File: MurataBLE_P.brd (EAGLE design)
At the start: 90 x 70 mm, 89 parts, among them CON1 C-2235, CON2 C-2235, IC1 I-5448, IC3 74LVC1G00DBV, IC5 I-5448, IC6 74LVC1G00DBV, Q1 FC-135 32.7680KA-AG3, Q2 12MHz, Q3 FC-135 32.7680KA-AG3, Q4 12MHz, SW1 P8073, SW2 P8073, SW3 P8073, SW4 P8073, SW5 P8073, SW6 P8073, U1 IC_BLE_LBCA2HNZYZ-711, U2 IC_BLE_LBCA2HNZYZ-711, X1 TSW-114-02-S-S, X2 TSW-114-02-S-S

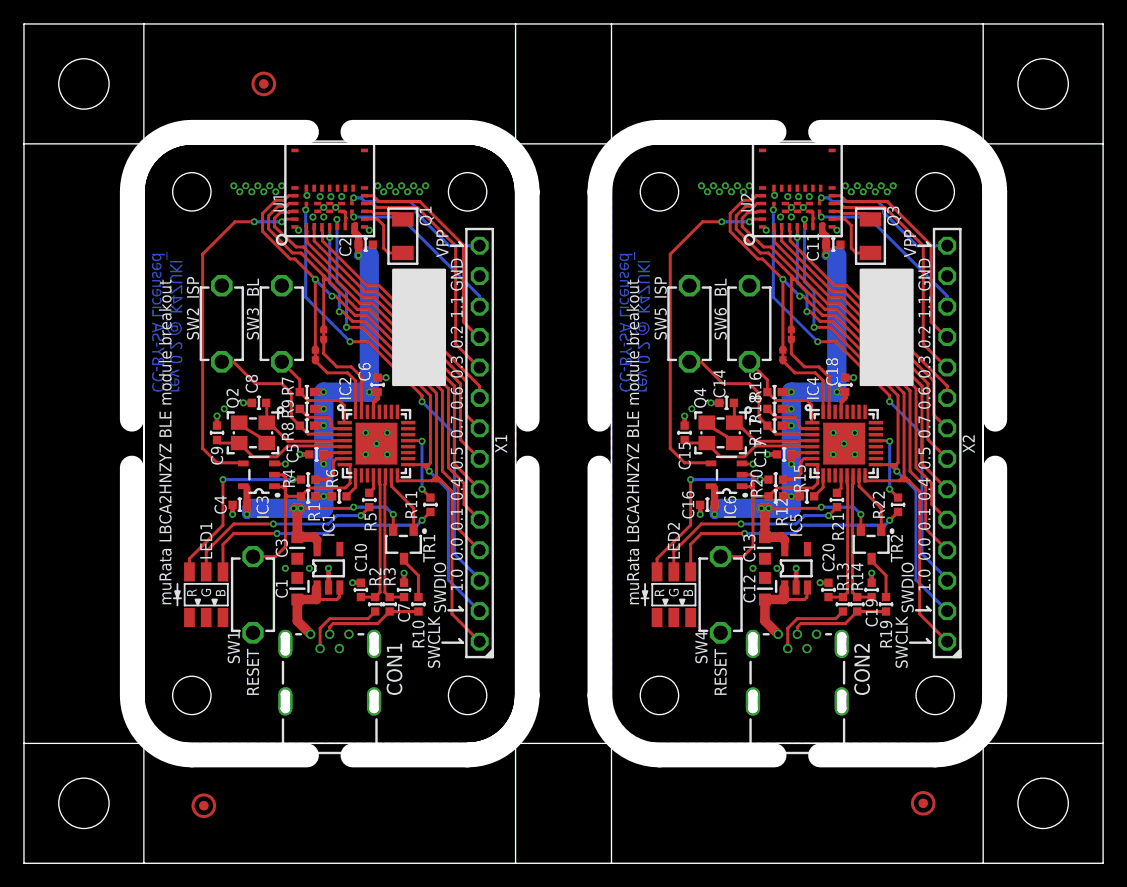
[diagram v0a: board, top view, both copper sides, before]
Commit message: [ USB ]add values; panelized
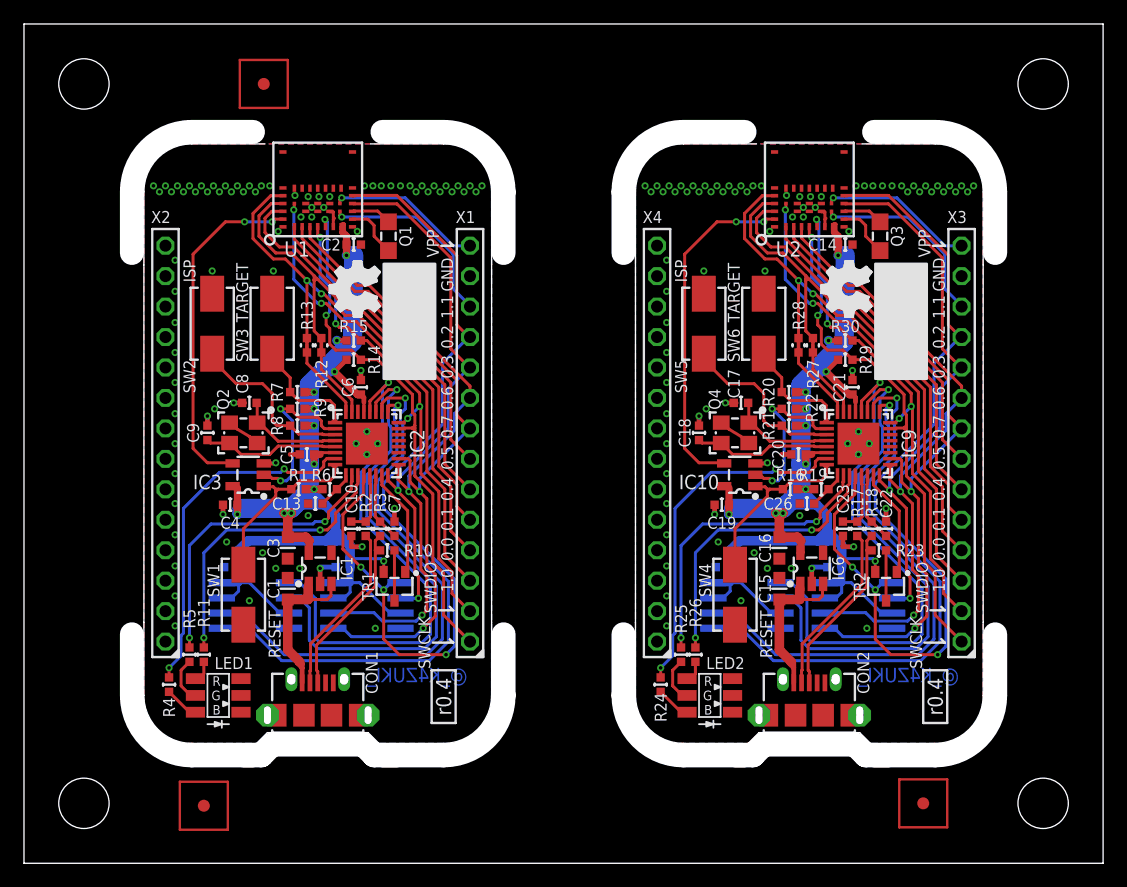
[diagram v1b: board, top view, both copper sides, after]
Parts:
- removed PCB1, PCB2: PCB_DP_RECTANGLE-31X50, dp_pcb:DP5031_V1
- removed TP1, TP16, TP17, TP18, TP19, TP2, TP3, TP4: TESTPAD, mylib:TP06RECT
- removed TP10, TP11, TP9: TPTP08R, testpad_local:TP08R
- removed TP12, TP13, TP14, TP15, TP5, TP6, TP7, TP8: TPTP06R, testpad_local:TP06R
- added C21, C24, C25, C26: 0.1u/1005, mylib:C0402
- added C22, C23: 18p/1005, mylib:C0402
- added GIT1: (no value), git-revision:GIT-REVISION
- added IC10: (no value), mylib:SOT95P280X145-5N
- added IC7, IC8: (no value), mylib:IC_08_1.27_150MIL
- added IC9: (no value), mylib:HVQFN33
- added ICON1, ICON3: r0.4, mylib:ICON_REVISION1.2
- added ICON2, ICON4: (no value), mylib:ICON_OSHW
- added P1, P2, P3, P4, P5, P6, P7, P8: (no value), mylib:PCB_CORNER_NH
- added R23: 1.5k/1005, mylib:C0402
- added R24, R25, R26: (no value), mylib:C0402
- added R27, R28: (no value), mylib:R0402SHORT
- added R29, R30: 10k/1005, mylib:C0402
- added TP100, TP101, TP102: TESTPAD_F, mylib:FIDUCIAL
- added X3, X4: TSW-114-02-S-S, mylib:TSW-114-07-F-S
- C12, C13: value 1u/1608 -> 0.1u/1005; device mylib:CR_1608 -> mylib:C0402
- C14, C19, C20: value 18p/1005 -> 0.1u/1005
- C15: value 18p/1005 -> 1u/1608; device mylib:C0402 -> mylib:CR_1608
- C16: value 0.1u/1005 -> 1u/1608; device mylib:C0402 -> mylib:CR_1608
- C17, C18: value 0.1u/1005 -> 18p/1005
- CON1, CON2: value C-2235 -> (none); device mylib:CON_USB_MINIB_AKI -> mylib:CON_USB_47589-0001MOLEX
- IC1: device mylib:IC_05_0.95_50MIL -> mylib:SOT95P280X145-5N
- IC3: value 74LVC1G00DBV -> (none); device 74xx-little-us_local:SOT23-5 -> mylib:SOT95P280X145-5N
- IC4: device mylib:HVQFN33 -> mylib:IC_08_1.27_150MIL
- IC5: value I-5448 -> (none); device mylib:IC_05_0.95_50MIL -> mylib:IC_08_1.27_150MIL
- IC6: value 74LVC1G00DBV -> I-5448; device 74xx-little-us_local:SOT23-5 -> mylib:SOT95P280X145-5N
- Q1, Q3: value FC-135 32.7680KA-AG3 -> (none); device mylib:CRYSTAL_FC-135 -> mylib:CR_2125
- Q2, Q4: value 12MHz -> (none); device adafruit (1):NX3225 -> mylib:CLOCK_3225
- R11, R5: value 75/1005 -> (none)
- R12: value 10k/1005 -> (none); device mylib:C0402 -> mylib:R0402SHORT
- R13: value 33/1005 -> (none); device mylib:C0402 -> mylib:R0402SHORT
- R14: value 33/1005 -> 10k/1005
- R17, R18: value 10k/1005 -> 33/1005
- R19: value 1.5k/1005 -> 10k/1005
- R20: value 270/1005 -> 10k/1005
- R21, R22: value 75/1005 -> 10k/1005
- R4: value 270/1005 -> (none)
- SW1, SW2, SW3, SW4, SW5, SW6: value P8073 -> (none); device mylib:SW_TACTSW_P8073 -> mylib:SW_TACTSW_FSM2JMTR
- TR1, TR2: value I-4269 -> PMOS_BSS84_SOT23
- U1, U2: value IC_BLE_LBCA2HNZYZ-711 -> (none)
- X1, X2: device mylib:TSW-114-02-S-S -> mylib:TSW-114-07-F-S
- moved X2 65.2 mm to (11.8, 35.0)
- moved IC4 50.9 mm to (19.3, 21.5), flipped to the bottom, turned to 270 degrees
- moved R13 49.6 mm to (23.6, 43.2)
- moved C11 49.0 mm to (26.6, 24.7), flipped to the bottom
- moved R14 46.7 mm to (27.5, 42.0), turned to 180 degrees
- moved C12 44.5 mm to (17.3, 24.7), flipped to the bottom, turned to 0 degrees
- moved R15 40.0 mm to (27.5, 43.6), turned to 180 degrees
- moved R12 39.9 mm to (24.8, 43.2), turned to 90 degrees
- moved C13 37.7 mm to (24.3, 30.0), turned to 180 degrees
- moved IC5 35.9 mm to (28.6, 21.5), flipped to the bottom, turned to 270 degrees
- moved R11 22.7 mm to (15.0, 17.4)
- moved R4 20.7 mm to (12.1, 14.9), turned to 270 degrees
- moved R5 19.8 mm to (13.8, 17.4)
- moved C14 16.5 mm to (68.5, 51.6), turned to 0 degrees
- moved C15 15.2 mm to (63.0, 22.9)
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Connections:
- net P0_4 renamed 580.P0_4
- net P0_5 renamed 580.P0_5
- net P1_0 renamed 580.P1_0
- removed net P0_10: U2.12, X2.11
- removed net P0_11: U2.11, X2.10
- removed net P0_12: U2.24, X2.6
- removed net P0_6: U1.3, X1.9
- removed net P0_7: U1.2, X1.8
- removed net P0_8: U2.3, X2.9
- removed net P0_9: U2.2, X2.8
- removed net P1_2: U2.35, X2.3
- removed net P1_3: U2.30, X2.12
- new net 580.P0_0: R12.3, U1.23, X1.5
- new net 580.P0_1: R13.3, U1.22, X1.4
- new net 580.P0_10: IC8.5, IC9.18, U2.2, X3.8
- new net 580.P0_11: IC8.1, IC9.12, U2.12, X3.11
- new net 580.P0_12: IC8.2, IC9.16, U2.11, X3.10
- new net 580.P0_13: U2.24, X3.6
- new net 580.P0_14: R27.3, U2.23, X3.5
- new net 580.P0_15: R28.3, U2.22, X3.4
- new net 580.P0_2: IC2.12, IC5.1, U1.12, X1.11
- new net 580.P0_3: IC2.16, IC5.2, U1.11, X1.10
- new net 580.P0_6: IC2.17, IC5.6, U1.3, X1.9
- new net 580.P0_7: IC2.18, IC5.5, U1.2, X1.8
- new net 580.P0_8: U2.1, X3.7
- new net 580.P0_9: IC8.6, IC9.17, U2.3, X3.9
- new net 580.P1_1: U1.30, X1.12
- new net 580.P1_2: U2.35, X3.3
- new net 580.P1_3: U2.30, X3.12
- new net P0_15: IC2.25, IC4.6
- new net P0_16: IC2.26, IC4.5
- new net P0_32: IC2.27, IC4.2
- new net P1_15: IC2.28, IC4.1
- net !RESET!: now also SW1.2; no longer IC3.2, SW1.A2
- net !RESET!1: now also IC10.1, IC9.8, R16.2, SW4.2; no longer IC4.8, IC6.1, IC6.2, R12.2, SW4.A2
- net 3.3V: now also C11.1, C12.1, IC4.3, IC4.7, IC4.8, IC5.3, IC5.7, IC5.8, R14.2, R15.2
- net 3.3V1: now also C14.1, C19.1, C20.1, C21.1, C24.1, C25.1, IC10.5, IC7.3, IC7.7, IC7.8, IC8.3, IC8.7, IC8.8, IC9.29, IC9.6, R19.1, R20.1, R21.1, R22.1, R29.2, R30.2; no longer C11.1, C13.1, C17.1, C18.1, IC4.29, IC4.6, IC5.5, R12.1, R15.1, R17.1, R18.1
- net FB_BL: now also SW3.2; no longer SW3.A2
- net FB_BL1: now also IC9.1, R20.2, SW6.2; no longer IC4.1, R16.2, SW6.A2
- net FB_ISP: now also SW2.2; no longer SW2.A2
- net FB_ISP1: now also IC9.3, R21.2, SW5.2; no longer IC4.3, R17.2, SW5.A2
- net GND: now also C11.2, C12.2, C13.2, CON1.5, CON1.SHD, CON1.SHD$1, CON1.SHD$2, CON1.SHD$3, CON1.SHD$4, CON1.SHD$5, CON1.SHD$6, CON1.SHD$7, IC4.4, IC5.4, SW1.1, SW2.1, SW3.1; no longer CON1.GND, SW1.A1, SW2.A1, SW3.A1
- net GND1: now also C21.2, C22.2, C23.2, C24.2, C25.2, C26.2, CON2.5, CON2.SHD, CON2.SHD$1, CON2.SHD$2, CON2.SHD$3, CON2.SHD$4, CON2.SHD$5, CON2.SHD$6, CON2.SHD$7, IC10.3, IC6.2, IC7.4, IC8.4, IC9.EXP, SW4.1, SW5.1, SW6.1, X3.13; no longer C11.2, C12.2, C13.2, CON2.GND, IC4.EXP, IC5.2, IC6.3, SW4.A1, SW5.A1, SW6.A1, X2.13
- net N$10: now also IC2.11; no longer IC2.21
- net N$16: now also C17.1, IC9.4; no longer C14.1, IC4.4
- net N$17: now also C18.1, IC9.5; no longer C15.1, IC4.5
- net N$21: now also CON1.3; no longer CON1.D+
- net N$22: now also CON1.2; no longer CON1.D-
- net N$23: now also CON2.3, R18.1, R23.2; no longer CON2.D+, R14.1, R19.2
- net N$25: now also CON2.2, R17.1; no longer CON2.D-, R13.1
- net N$26: now also C22.1, IC9.14, R18.2; no longer C19.1, IC4.14, R14.2
- net N$27: now also C23.1, IC9.13, R17.2; no longer C20.1, IC4.13, R13.2
- net N$28: now also C26.1, IC9.9, R19.2; no longer IC4.9, R15.2
- net N$29: now also IC10.2, IC9.2, R22.2; no longer IC4.2, R18.2
- net N$30: now also R23.1; no longer R19.1
- net N$31: now also IC9.15; no longer IC4.15
- net N$32: now also IC9.7, R24.1; no longer IC4.7, R20.1
- net N$33: now also IC9.10, R25.1; no longer IC4.12, R21.1
- net N$34: now also IC9.11, R26.1; no longer IC4.21, R22.1
- net N$35: now also R24.2; no longer R20.2
- net N$36: now also R25.2; no longer R21.2
- net N$37: now also R26.2; no longer R22.2
- net N$4: now also C13.1
- net N$5: now also IC3.2
- net N$9: now also IC2.10; no longer IC2.12
- net P0_1: now also IC7.2, IC9.27; no longer U2.1, X2.7
- net P0_2: now also IC7.5, IC9.26; no longer U1.12, X1.11
- net P0_3: now also IC7.6, IC9.25; no longer U1.11, X1.10
- net P1_1: now also IC7.1, IC9.28; no longer U1.30, X1.12
- net RESET1: now also IC10.4; no longer IC6.4
- net SWCLK: now also IC2.23, R14.1; no longer IC2.16
- net SWCLK1: now also IC9.23, R29.1, X3.1; no longer IC4.16, X2.1
- net SWDIO: now also IC2.24, R15.1; no longer IC2.17
- net SWDIO1: now also IC9.24, R30.1, X3.2; no longer IC4.17, X2.2
- net TGT_RX: now also R13.1, R13.2; no longer TP2.TP, TP4.TP, TP6.TP, TP7.TP, U1.22, X1.4
- net TGT_RX1: now also IC9.32, R28.1, R28.2; no longer IC4.32, TP13.TP, TP14.TP, TP17.TP, TP19.TP, U2.22, X2.4
- net TGT_TX: now also R12.1, R12.2; no longer TP1.TP, TP3.TP, TP5.TP, TP8.TP, U1.23, X1.5
- net TGT_TX1: now also IC9.31, R27.1, R27.2; no longer IC4.31, TP12.TP, TP15.TP, TP16.TP, TP18.TP, U2.23, X2.5
- net VPP1: now also X3.14; no longer X2.14
- net VUSB: now also CON1.1; no longer CON1.VBUS
- net VUSB1: now also C15.1, CON2.1, IC6.1, IC6.3; no longer C12.1, CON2.VBUS, IC5.1, IC5.3
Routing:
- net 580.P0_2: track 0.00 -> 73.6 mm, vias 0 -> 3
- net 580.P0_11: track 0.00 -> 73.6 mm, vias 0 -> 3
- net 580.P0_10: track 0.00 -> 54.7 mm, vias 0 -> 2
- net 580.P0_7: track 0.00 -> 54.7 mm, vias 0 -> 2
- net 580.P0_9: track 0.00 -> 52.6 mm, vias 0 -> 2
- net 580.P0_6: track 0.00 -> 52.6 mm, vias 0 -> 2
- net P0_16: track 0.00 -> 47.4 mm, vias 0 -> 1
- net TGT_RX1: track 53.3 -> 6.90 mm, vias 2 -> 0
- net TGT_RX: track 53.3 -> 6.90 mm, vias 2 -> 0
- net 580.P0_3: track 0.00 -> 45.6 mm, vias 0 -> 2
- net 580.P0_12: track 0.00 -> 45.6 mm, vias 0 -> 2
- net 580.P0_15: track 0.00 -> 44.9 mm, vias 0 -> 2
- net 580.P0_1: track 0.00 -> 44.9 mm, vias 0 -> 2
- net P0_15: track 0.00 -> 44.7 mm, vias 0 -> 1
- net P1_15: track 0.00 -> 43.7 mm, vias 0 -> 1
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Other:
- outline, holes or cut-outs redrawn
- board text added: "@_K4ZUKI_"
- board text added: "C11"
- board text added: "C12"
- board text added: "C13"
- board text added: "IC4"
- board text added: "IC5"
- board text added: "R12"
- board text added: "R13"
- board text added: "R14"
- board text added: "R15"
- board text added: "TARGET"
- board text added: "V-CUT"
- board text added: "X2"
- board text removed: "BL"
- board text removed: "CC-BY-SA Licensed"
- board text removed: "rev 0.2 @_K4ZUKI_"

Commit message: [ USB ] GERBER as per aef7891
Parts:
- added GIT2: aef7891, git-revision:GIT-REVISION
- added LED3, LED4: LED_3SEG, mylib:LED_3SEG_SMD
- added R31: NC, mylib:R0402SHORT
- added R32, R33: 10k/1005, mylib:C0402
- added R34, R35, R36: 1k/1005, mylib:C0402
- CON1, CON2: value (none) -> 47589-0001
- GIT1: value (none) -> aef7891
- IC1: value I-5448 -> (none); device mylib:SOT95P280X145-5N -> mylib:DFN80P410X410_8N
- IC10: device mylib:SOT95P280X145-5N -> mylib:DFN80P410X410_8N
- IC2: value (none) -> LPC11U35_QFN33
- IC3: value (none) -> NC7SZ00
- IC4: value (none) -> AT25DN512C
- IC5, IC7: value (none) -> AT25XE011
- IC6: value I-5448 -> AT25DN512C; device mylib:SOT95P280X145-5N -> mylib:IC_08_1.27_150MIL
- IC8: value (none) -> LPC11U35_QFN33; device mylib:IC_08_1.27_150MIL -> mylib:HVQFN33
- IC9: value (none) -> NC7SZ00; device mylib:HVQFN33 -> mylib:SOT95P280X145-5N
- ICON2, ICON4, P1, P2, P3, P4, P5, P6, P7, P8, R12, R13: value (none) -> NC
- Q1, Q3: value (none) -> 32.768K/2012
- Q2, Q4: value (none) -> 12M/3225
- R11, R4, R5: value (none) -> 1k/1005
- R16, R29: value 10k/1005 -> 1k/1005
- R17, R18: value 33/1005 -> 1k/1005
- R20, R21: value 10k/1005 -> 33/1005
- R23: value 1.5k/1005 -> 10k/1005
- R24, R25: value (none) -> 10k/1005
- R26: value (none) -> 1.5k/1005
- R27, R28: value (none) -> 1k/1005; device mylib:R0402SHORT -> mylib:C0402
- R30: value 10k/1005 -> NC; device mylib:C0402 -> mylib:R0402SHORT
- SW1, SW2, SW3, SW4, SW5, SW6: value (none) -> FSM2JMTR
- TP100, TP101, TP102: value TESTPAD_F -> NC
- TR1, TR2: value PMOS_BSS84_SOT23 -> BSS84
- U1, U2: value (none) -> LBCA2HNZYZ
- moved R18 64.3 mm to (11.9, 53.9), turned to 180 degrees
- moved R17 61.1 mm to (14.8, 55.1), turned to 180 degrees
- moved R16 57.2 mm to (11.9, 55.1)
- moved LED2 56.2 mm to (16.1, 52.4), turned to 0 degrees
- moved GIT1 35.1 mm to (32.2, 13.9), turned to 90 degrees
- moved R24 24.1 mm to (63.8, 36.5), turned to 180 degrees
- moved R27 23.5 mm to (54.8, 22.4), turned to 270 degrees
- moved R25 22.4 mm to (63.8, 37.9), turned to 180 degrees
- moved R29 20.9 mm to (56.0, 25.3), turned to 270 degrees
- moved R28 20.4 mm to (54.8, 25.3), turned to 270 degrees
- moved R26 17.6 mm to (71.3, 26.1), turned to 180 degrees
- moved R23 15.2 mm to (63.8, 39.3)
- moved IC8 13.5 mm to (69.6, 35.0), flipped to the top, turned to 0 degrees
- moved R20 12.7 mm to (69.5, 27.9), turned to 90 degrees
- moved R21 11.0 mm to (70.7, 27.9), turned to 90 degrees
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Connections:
- net VPP1 renamed VPP2
- removed net N$17 (its old number): C18.1, IC9.5, Q4.3
- removed net N$5 (its old number): IC2.2, IC3.2, R9.2
- new net N$14: LED2.3, R18.1
- new net N$15: LED2.2, R17.1
- new net N$38: LED3.3, R27.2
- new net N$39: LED4.3, R36.1
- new net N$40: LED4.2, R35.1
- new net N$41: LED4.1, R34.1
- new net NSRST: IC2.8, IC3.1, IC3.2, R1.2
- new net NSRST1: IC8.8, IC9.1, IC9.2, R19.2
- net !RESET!: now also IC2.2, R9.2; no longer IC2.8, IC3.1, R1.2
- net !RESET!1: now also IC8.2, R25.2; no longer IC10.1, IC9.8, R16.2
- net 3.3V: now also IC1.6, IC1.7, IC1.EP, LED1.4, LED1.5, LED1.6, X2.1
- net 3.3V1: now also IC10.6, IC10.7, IC10.EP, IC6.3, IC6.7, IC6.8, IC8.29, IC8.6, IC9.5, LED3.4, LED3.5, LED3.6, R23.1, R24.1, R25.1, R32.2, R33.2, X4.1; no longer IC6.5, IC8.3, IC8.7, IC8.8, IC9.29, IC9.6, R16.1, R20.1, R21.1, R29.2, R30.2
- net 580.P0_0: now also LED2.4
- net 580.P0_1: now also LED2.5
- net 580.P0_10: now also IC7.5, IC8.18; no longer IC8.5, IC9.18
- net 580.P0_11: now also IC7.1, IC8.12; no longer IC8.1, IC9.12
- net 580.P0_12: now also IC7.2, IC8.16; no longer IC8.2, IC9.16
- net 580.P0_14: now also LED4.4, R30.3; no longer R27.3
- net 580.P0_15: now also LED4.5, R31.3; no longer R28.3
- net 580.P0_9: now also IC7.6, IC8.17; no longer IC8.6, IC9.17
- net 580.P1_0: now also LED2.6
- net 580.P1_2: now also LED4.6
- net FB_BL1: now also IC8.1, R23.2; no longer IC9.1, R20.2
- net FB_ISP1: now also IC8.3, R24.2; no longer IC9.3, R21.2
- net GND: now also IC1.1, R16.2, R17.2, R18.2; no longer IC1.2, LED1.1, LED1.2, LED1.3
- net GND1: now also IC10.1, IC6.4, IC8.EXP, IC9.3, R34.2, R35.2, R36.2; no longer IC10.3, IC6.2, IC8.4, IC9.EXP, LED2.1, LED2.2, LED2.3
- net N$11: now also LED1.1, R11.2; no longer LED1.4, R4.2
- net N$12: now also LED1.2; no longer LED1.5
- net N$13: now also LED1.3, R4.2; no longer LED1.6, R11.2
- net N$16: now also LED2.1, R16.1; no longer C17.1, IC9.4, Q4.1
- net N$23: now also C17.1, IC8.4, Q4.1; no longer CON2.3, R18.1, R23.2
- net N$25: now also C18.1, IC8.5, Q4.3; no longer CON2.2, R17.1
- net N$26: now also CON2.3, R21.1, R26.2; no longer C22.1, IC9.14, R18.2
- net N$27: now also CON2.2, R20.1; no longer C23.1, IC9.13, R17.2
- net N$28: now also C22.1, IC8.14, R21.2; no longer C26.1, IC9.9, R19.2
- net N$29: now also C23.1, IC8.13, R20.2; no longer IC10.2, IC9.2, R22.2
- net N$30: now also C26.1, IC8.9, R22.2; no longer R23.1, TR2.3
- net N$31: now also R26.1, TR2.3; no longer IC9.15, TR2.1
- net N$32: now also IC8.15, TR2.1; no longer IC9.7, R24.1
- net N$33: now also IC8.7, R27.1; no longer IC9.10, R25.1
- net N$34: now also IC8.10, R28.1; no longer IC9.11, R26.1
- net N$35: now also IC8.11, R29.1; no longer LED2.4, R24.2
- net N$36: now also LED3.2, R28.2; no longer LED2.5, R25.2
- net N$37: now also LED3.1, R29.2; no longer LED2.6, R26.2
- net P0_1: now also IC6.2, IC8.27; no longer IC7.2, IC9.27
- net P0_2: now also IC6.5, IC8.26; no longer IC7.5, IC9.26
- net P0_3: now also IC6.6, IC8.25; no longer IC7.6, IC9.25
- net P1_1: now also IC6.1, IC8.28; no longer IC7.1, IC9.28
- net RESET1: now also IC9.4; no longer IC10.4
- net SWCLK1: now also IC8.23, R32.1; no longer IC9.23, R29.1
- net SWDIO1: now also IC8.24, R33.1; no longer IC9.24, R30.1
- net TGT_RX1: now also IC8.32, R31.1, R31.2; no longer IC9.32, R28.1, R28.2
- net TGT_TX1: now also IC8.31, R30.1, R30.2; no longer IC9.31, R27.1, R27.2
- net VUSB: now also IC1.2, IC1.4; no longer IC1.1
- net VUSB1: now also IC10.2, IC10.3, IC10.4; no longer IC6.1, IC6.3
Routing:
- net 3.3V1: track 107.9 -> 136.6 mm, vias 12 -> 13
- net 3.3V: track 107.9 -> 136.6 mm, vias 12 -> 13
- net N$32: track 29.4 -> 9.02 mm, vias 2 -> 0
- net N$5 (its old number): track 14.2 -> 0.00 mm, vias 2 -> 0
- net N$35: track 2.90 -> 16.8 mm, vias 0 -> 2
- net N$17 (its old number): track 11.5 -> 0.00 mm
- net N$38: track 0.00 -> 10.7 mm
- net NSRST: track 0.00 -> 9.99 mm
- net NSRST1: track 0.00 -> 9.99 mm
- net N$27: track 5.24 -> 14.5 mm
- net N$26: track 5.73 -> 14.9 mm
- net N$29: track 14.2 -> 5.24 mm, vias 2 -> 0
- net N$13: track 1.87 -> 10.7 mm
- net N$36: track 3.82 -> 12.3 mm
- net N$12: track 3.82 -> 12.3 mm
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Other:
- board text added: "3.3V"
- board text added: "LED2"
- board text added: "R16"
- board text added: "R17"
- board text added: "R18"
